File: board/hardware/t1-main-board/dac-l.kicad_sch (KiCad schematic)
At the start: 26 parts, among them U2501 CS43198-CNZR, U2502 TPS7A2018PDBVR

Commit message: Board: capture blk.debug
Debug UART2 (1.8 V) and I2S/DSD pads with ground pads, reset, PMIC and
power-key pads (PCB-T-09), a pad on every spare SoC GPIO whose pinout v1
row names one (the DEBUG bus, on the SoC's right edge), and a rail pad
for each power-tree rail no other sheet probes (PCB-T-02). Each DAC
sheet carries a pad on its MCLK. The spares pinout v1 leaves without a
pad now carry no-connect flags. On the root, facing sheet pins are
joined directly only where the route meets no other symbol.

Co-Authored-By: Claude Opus 5.5 <noreply@anthropic.com>
Claude-Session: https://claude.ai/code/session_01Ei262h3TpgY9vyfNLMi5Mn
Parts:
- added TP2503: MCLK_L, TestPoint:TestPoint_Pad_D1.0mm, symbol Connector:TestPoint
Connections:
- net MCLK_L: now also TP2503.1
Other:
- note added: "MCLK test pad (BOM v1 line 88)"
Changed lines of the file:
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@@
 (rectangle (start 22.86 163.83) (end 250.19 214.63) (stroke (width 0) (type dash)) (fill (type none)))
 (text "Supplies and charge pumps (Fig. 2-1)" (exclude_from_sim no) (at 24.13 162.56 0) (effects (font (size 2.54 2.54)) (justify left bottom)))
+(symbol (lib_id "Connector:TestPoint") (at 220.98 140.97 0) (unit 1) (body_style 1) (exclude_from_sim no) (in_bom no) (on_board yes) (dnp no)
+  (property "Reference" "TP2503" (at 219.71 135.89 0) (effects (font (size 1.27 1.27)) (justify right)))
+  (property "Value" "MCLK_L" (at 219.71 138.43 0) (effects (font (size 1.27 1.27)) (justify right)))
+  (property "Footprint" "TestPoint:TestPoint_Pad_D1.0mm" (at 220.98 140.97 0) (effects (font (size 1.27 1.27))) (hide yes))
+  (property "Datasheet" "~" (at 220.98 140.97 0) (effects (font (size 1.27 1.27))) (hide yes))
+  (property "Description" "Test pad, 1.0 mm" (at 220.98 140.97 0) (effects (font (size 1.27 1.27))) (hide yes))
+  (property "Block" "blk.dac-l" (at 220.98 140.97 0) (effects (font (size 1.27 1.27))) (hide yes))
+  (pin "1")
+  (instances (project "t1-main-board" (path "/7746052e-d7f9-59ad-ba73-bd2b74439529/d6f0155c-678f-5298-bf09-6ea7c0e72438/d1d91382-bca7-5fb9-8b3a-5a4997a5678f" (reference "TP2503") (unit 1))))
+)
+(rectangle (start 209.55 130.81) (end 280.67 152.4) (stroke (width 0) (type dash)) (fill (type none)))
+(text "MCLK test pad (BOM v1 line 88)" (exclude_from_sim no) (at 210.82 129.54 0) (effects (font (size 2.54 2.54)) (justify left bottom)))
 (text_box "Notes\n1. Function: Cirrus Logic CS43198 for the left channel in mono mode (dual mono, BOM v1\n   line 18): AOUTA and AOUTB a differential pair into both output stages; I2C2 address 0x30 (ADR to ground).\n2. Absent state: never omitted (T1-040). RESET held low by the host-side pull-down; INT pulled\n   up only on DAC_DIG_1V8; I2C isolated while DAC_DIG_1V8 is off (G2).\n3. Clock master: SCLK1 and LRCK1 drive I2S_BCLK and I2S_LRCK through 22 Ω (HDG p. 70).\n   XTI/MCLK from its own divider (blk.mclk); XTO, CLKOUT, TSO and DSDB/LRCK2 unused.\n   DSD: DSDA from DSD_x, DSDCLK from I2S_BCLK (native DSD reserved, blackbird-os ADR 0006).\n4. HP_DETECT tied low: plug detection is on the jacks (expander P10, P11).\n5. VA from its own TPS7A2018 (EN = AUDIO_LN_EN) behind link L1; VL, VD, VCP on DAC_DIG_1V8;\n   VP on DAC_VP (PCB-A-05). GNDA, GNDCP, GNDD and the pad in one ground (PCB-A-01, -02).\n6. Open: series values other than 0 Ω (bring-up, G2); CS43198 pins fail-safe unpowered (UNVERIFIED)." (exclude_from_sim no) (at 275.59 219.71 0) (size 129.54 29.21) (margins 1.905 1.905 1.905 1.905) (stroke (width 0) (type default)) (fill (type none)) (effects (font (size 1.27 1.27)) (justify left top)))
 (text "Interface" (exclude_from_sim no) (at 22.86 226.06 0) (effects (font (size 2.54 2.54)) (justify left bottom)))
@@
 (label "DACL_FLYN_VCP" (at 236.22 193.04 270) (effects (font (size 1.27 1.27)) (justify right bottom)))
 (label "DACL_FLYC_VCP" (at 236.22 182.88 90) (effects (font (size 1.27 1.27)) (justify left bottom)))
+(hierarchical_label "MCLK_L" (shape input) (at 220.98 140.97 270) (effects (font (size 1.27 1.27)) (justify right)))
 (bus (pts (xy 45.72 219.71) (xy 50.8 219.71)) (stroke (width 0) (type default)))
 (hierarchical_label "{AUDIO_CTL}" (shape bidirectional) (at 45.72 219.71 180) (effects (font (size 1.27 1.27)) (justify right)))

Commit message: Board on libs v0.2.0: lower-case kebab vendor keys (HL-13)
The libs submodule moves to v0.2.0 (5f24483). Every library nickname in
the generator, the placement tool and the floorplan study follows the
key table (Texas_Instruments -> texas-instruments, OpenDAP_Device ->
opendap-generic, Rockchip and Rockchip_PMIC -> rockchip, ...); the
library tables are written from the files. Schematic and board
regenerated.

Checks: ERC 0 errors (warnings unchanged); DRC 0 errors, 605 warnings,
the same counts by type, schematic parity 0; every placement identical;
craft Q1 met; pcb tests pass; STEP export resolves every libs 3D model
(the 27 parts without a model are KiCad stock lands that have none).

Co-Authored-By: Claude Opus 5.5 <noreply@anthropic.com>
Claude-Session: https://claude.ai/code/session_01Ei262h3TpgY9vyfNLMi5Mn
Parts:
- U2501: footprint Cirrus_Logic:QFN-40-1EP_5x5mm_P0.4mm_EP3.5x3.5mm_ThermalVias -> cirrus-logic:QFN-40-1EP_5x5mm_P0.4mm_EP3.5x3.5mm_ThermalVias; symbol Cirrus_Logic:CS43198-CNZR -> cirrus-logic:CS43198-CNZR
- U2502: footprint Texas_Instruments:Texas_DBV0005A_SOT-23-5_1.6x2.9mm_P0.95mm -> texas-instruments:Texas_DBV0005A_SOT-23-5_1.6x2.9mm_P0.95mm; symbol Texas_Instruments:TPS7A2018PDBVR -> texas-instruments:TPS7A2018PDBVR
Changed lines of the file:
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@@
 (rectangle (start 22.86 35.56) (end 105.41 114.3) (stroke (width 0) (type dash)) (fill (type none)))
 (text "Serial port (BOM v1 lines 134, 141)" (exclude_from_sim no) (at 24.13 34.29 0) (effects (font (size 2.54 2.54)) (justify left bottom)))
-(symbol (lib_id "Cirrus_Logic:CS43198-CNZR") (at 149.86 101.6 0) (unit 1) (body_style 1) (exclude_from_sim no) (in_bom yes) (on_board yes) (dnp no)
+(symbol (lib_id "cirrus-logic:CS43198-CNZR") (at 149.86 101.6 0) (unit 1) (body_style 1) (exclude_from_sim no) (in_bom yes) (on_board yes) (dnp no)
   (property "Reference" "U2501" (at 158.75 62.23 0) (effects (font (size 1.27 1.27)) (justify left)))
   (property "Value" "CS43198-CNZR" (at 158.75 59.69 0) (effects (font (size 1.27 1.27)) (justify left)))
-  (property "Footprint" "Cirrus_Logic:QFN-40-1EP_5x5mm_P0.4mm_EP3.5x3.5mm_ThermalVias" (at 149.86 101.6 0) (effects (font (size 1.27 1.27))) (hide yes))
+  (property "Footprint" "cirrus-logic:QFN-40-1EP_5x5mm_P0.4mm_EP3.5x3.5mm_ThermalVias" (at 149.86 101.6 0) (effects (font (size 1.27 1.27))) (hide yes))
   (property "Datasheet" "https://www.cirrus.com/docs/ds/cs43198-datasheet.pdf" (at 149.86 101.6 0) (effects (font (size 1.27 1.27))) (hide yes))
   (property "Description" "Stereo 32-bit audio DAC with pseudodifferential headphone-capable outputs, 40-pin QFN 5 x 5 mm, 0.4 mm pitch, exposed pad" (at 149.86 101.6 0) (effects (font (size 1.27 1.27))) (hide yes))
@@
   (instances (project "t1-main-board" (path "/7746052e-d7f9-59ad-ba73-bd2b74439529/d6f0155c-678f-5298-bf09-6ea7c0e72438/d1d91382-bca7-5fb9-8b3a-5a4997a5678f" (reference "#FLG0021") (unit 1))))
 )
-(symbol (lib_id "Texas_Instruments:TPS7A2018PDBVR") (at 238.76 93.98 0) (unit 1) (body_style 1) (exclude_from_sim no) (in_bom yes) (on_board yes) (dnp no)
+(symbol (lib_id "texas-instruments:TPS7A2018PDBVR") (at 238.76 93.98 0) (unit 1) (body_style 1) (exclude_from_sim no) (in_bom yes) (on_board yes) (dnp no)
   (property "Reference" "U2502" (at 231.14 78.74 0) (effects (font (size 1.27 1.27)) (justify left)))
   (property "Value" "TPS7A2018PDBVR" (at 231.14 76.2 0) (effects (font (size 1.27 1.27)) (justify left)))
-  (property "Footprint" "Texas_Instruments:Texas_DBV0005A_SOT-23-5_1.6x2.9mm_P0.95mm" (at 238.76 93.98 0) (effects (font (size 1.27 1.27))) (hide yes))
+  (property "Footprint" "texas-instruments:Texas_DBV0005A_SOT-23-5_1.6x2.9mm_P0.95mm" (at 238.76 93.98 0) (effects (font (size 1.27 1.27))) (hide yes))
   (property "Datasheet" "https://www.ti.com/lit/ds/symlink/tps7a20.pdf" (at 238.76 93.98 0) (effects (font (size 1.27 1.27))) (hide yes))
   (property "Description" "LDO regulator, 300 mA, 1.8 V fixed, 7 uVrms noise, 95 dB PSRR at 1 kHz, active output discharge, SOT-23-5 (DBV0005A)" (at 238.76 93.98 0) (effects (font (size 1.27 1.27))) (hide yes))

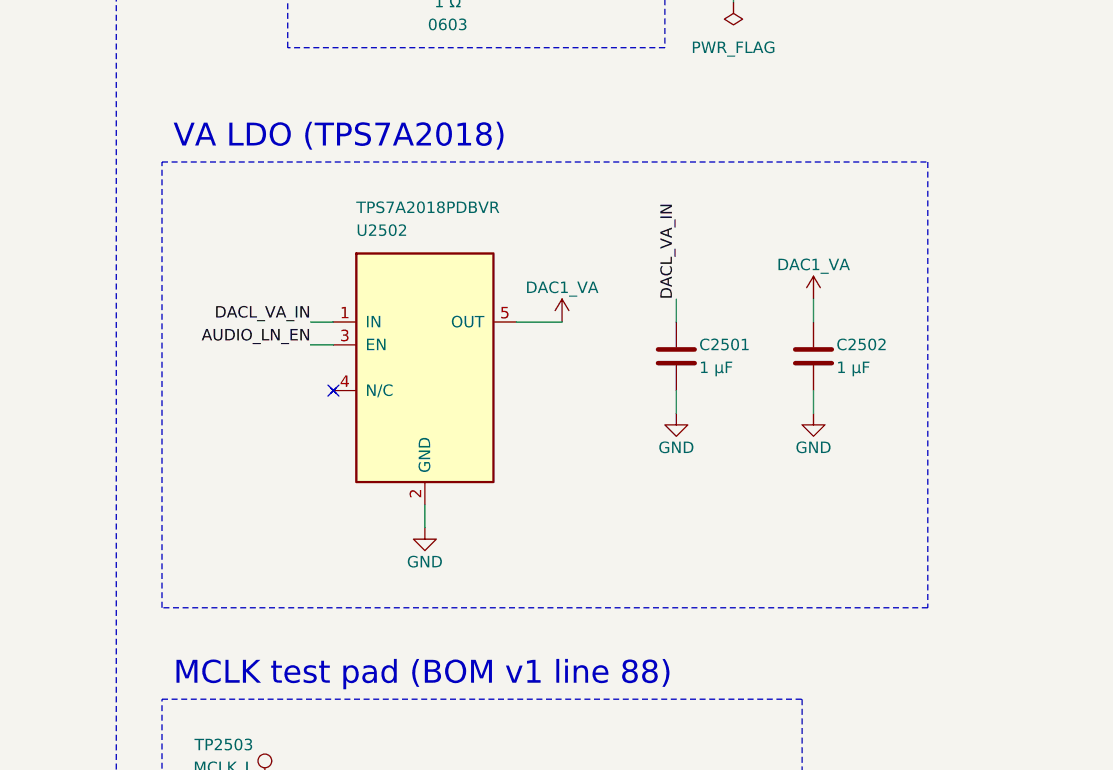
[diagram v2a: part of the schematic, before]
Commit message: BOM v1.18 item 2: successors of the discontinued 1 uF 0402
GRM155R61A105KE15D is to be discontinued. 44 positions take
GRM155C71A105KE11D (1 uF 10 V X7S); the eight TPS7A20 positions take
GRM155R61C225KE11D (2.2 uF 16 V X5R) to keep the 0.47 uF effective
minimum with 10 % to spare at up to 3.8 V. Same land; sourcing pass.
Closes BOM §7 item 52; new item 55 lists the other capture parts outside
Murata's product data or near end of life.

Co-Authored-By: Claude Opus 5.5 <noreply@anthropic.com>
Claude-Session: https://claude.ai/code/session_01Ei262h3TpgY9vyfNLMi5Mn
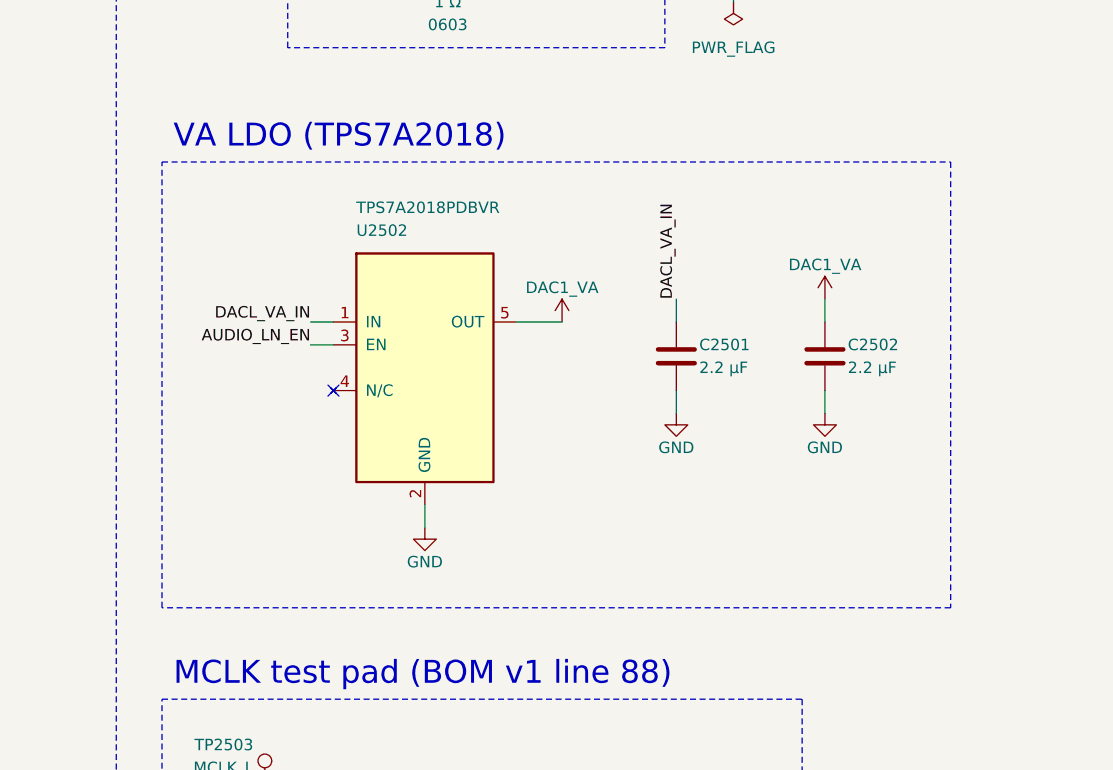
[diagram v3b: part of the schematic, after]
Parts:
- C2501, C2502: value 1 µF -> 2.2 µF; MPN GRM155R61A105KE15D -> GRM155R61C225KE11D
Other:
- moved on the sheet: C2502
